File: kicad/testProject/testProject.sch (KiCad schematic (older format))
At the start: 13 parts, among them U1 74HC86

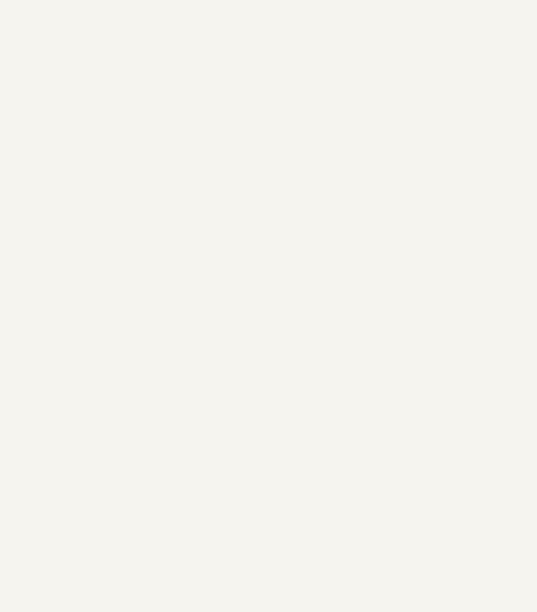
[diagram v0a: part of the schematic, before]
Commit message: Finished writing digital devices pt 2.
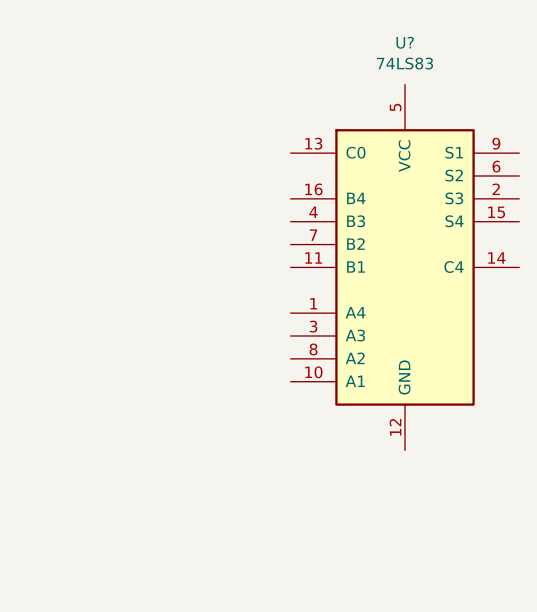
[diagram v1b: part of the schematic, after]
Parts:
- added U?: 74LS83, symbol 74xx:74LS83
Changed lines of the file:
@@
 EESchema Schematic File Version 4
+LIBS:testProject-cache
 EELAYER 29 0
 EELAYER END
@@
 	4250 5150 4250 5700
 Connection ~ 4250 5700
+$Comp
+L 74xx:74LS83 U?
+U 1 1 5D212947
+P 9000 2850
+F 0 "U?" H 9000 3831 50  0000 C CNN
+F 1 "74LS83" H 9000 3740 50  0000 C CNN
+F 2 "" H 9000 2850 50  0001 C CNN
+F 3 "http://www.ti.com/lit/gpn/sn74LS83" H 9000 2850 50  0001 C CNN
+	1    9000 2850
+	1    0    0    -1
+$EndComp
 $EndSCHEMATC
